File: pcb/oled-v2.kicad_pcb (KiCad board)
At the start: 2 copper layers, 89.5 x 39.5 mm, 26 parts, among them J1 OLED_128x32, U1 MOUDLE-SEEEDUINO-XIAO

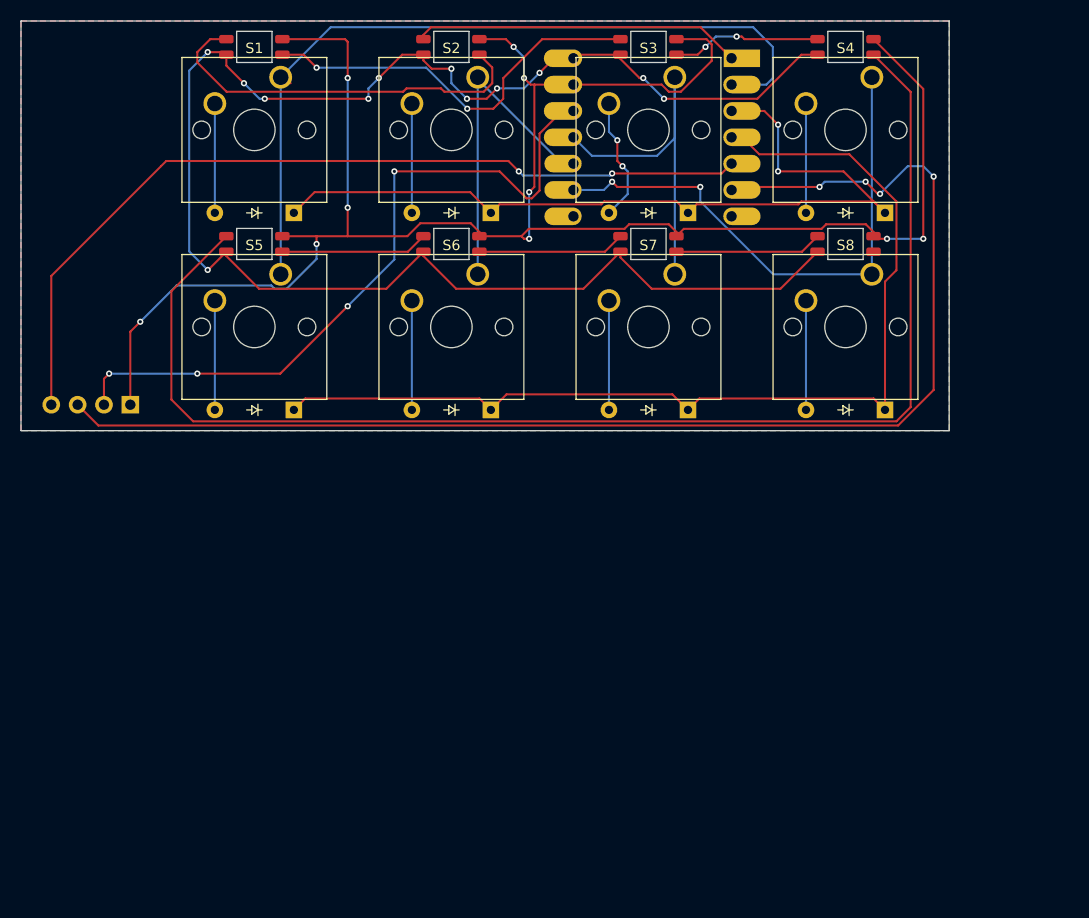
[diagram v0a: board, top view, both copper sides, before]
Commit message: turns out I had my GND wired to 5V - fixed now.
production/oled-v2.3mf = full CAD file
images updated
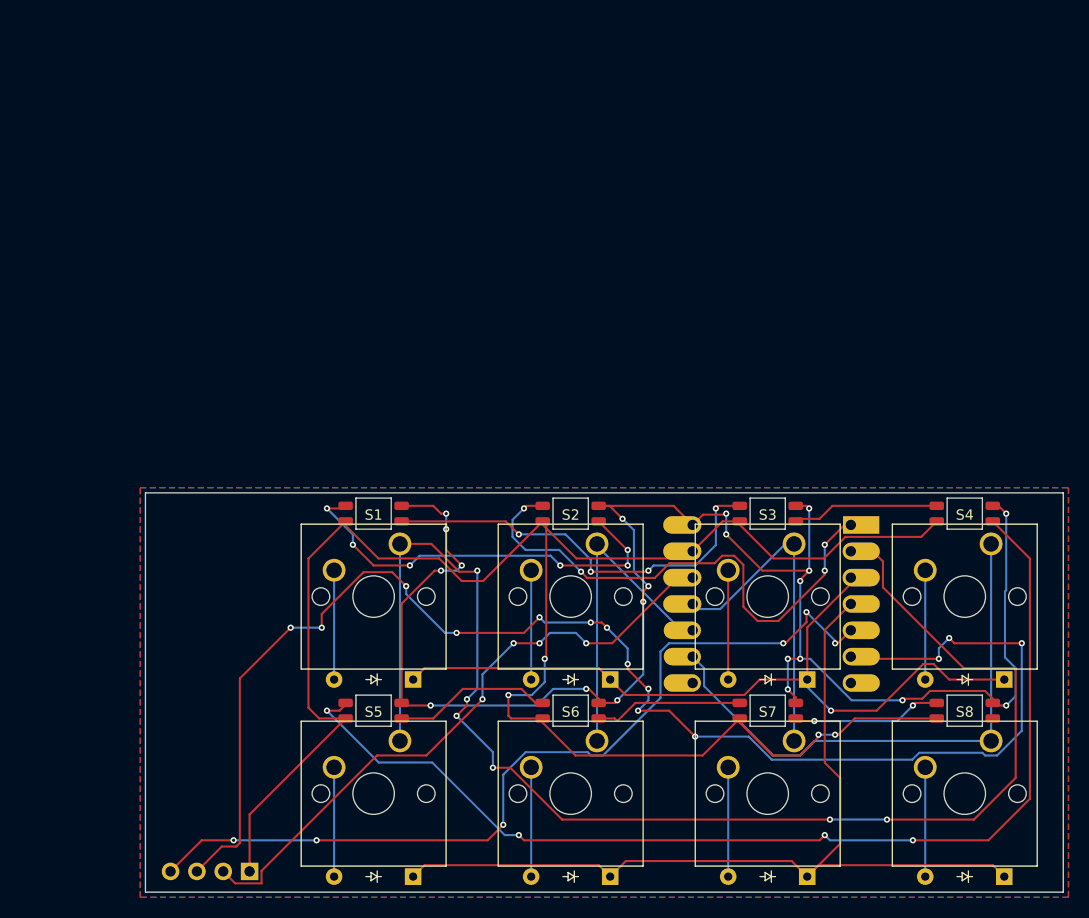
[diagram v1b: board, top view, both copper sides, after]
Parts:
- moved D1 46.4 mm to (99.3, 116.0)
- moved D10 46.4 mm to (114.5, 100.0)
- moved D11 46.4 mm to (133.5, 100.0)
- moved D12 46.4 mm to (152.5, 100.0)
- moved D13 46.4 mm to (95.5, 119.0)
- moved D14 46.4 mm to (114.5, 119.0)
- moved D15 46.4 mm to (133.5, 119.0)
- moved D16 46.4 mm to (152.5, 119.0)
- moved D2 46.4 mm to (118.3, 116.0)
- moved D3 46.4 mm to (137.3, 116.0)
- moved D4 46.4 mm to (156.3, 116.0)
- moved D5 46.4 mm to (99.3, 135.0)
- moved D6 46.4 mm to (118.3, 135.0)
- moved D7 46.4 mm to (137.3, 135.0)
- moved D8 46.4 mm to (156.3, 135.0)
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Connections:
- D10 pad 1: LED_GND -> 5V
- D10 pad 3: 5V -> LED_GND
- D11 pad 1: LED_GND -> 5V
- D11 pad 3: 5V -> LED_GND
- D12 pad 1: LED_GND -> 5V
- D12 pad 3: 5V -> LED_GND
- D13 pad 1: LED_GND -> 5V
- D13 pad 3: 5V -> LED_GND
- D14 pad 1: LED_GND -> 5V
- D14 pad 3: 5V -> LED_GND
- D15 pad 1: LED_GND -> 5V
- D15 pad 3: 5V -> LED_GND
- D16 pad 1: LED_GND -> 5V
- D16 pad 3: 5V -> LED_GND
- D9 pad 1: LED_GND -> 5V
- D9 pad 3: 5V -> LED_GND
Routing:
- net Col 0: track 77.7 -> 135.6 mm, vias 0 -> 6
- net Net-(D12-DOUT): track 126.1 -> 105.9 mm, vias 0 -> 4
- net LED0_DIN: track 31.7 -> 50.7 mm, vias 0 -> 4
- net OLED_SCL: track 127.2 -> 142.6 mm, vias 4 -> 14
- net LED_GND: track 190.8 -> 180.0 mm, vias 10 -> 4
- net Row 1: track 99.1 -> 89.3 mm
- net OLED_VCC: track 68.8 -> 60.9 mm
- net Row 0: track 82.0 -> 74.9 mm, vias 2 -> 1
- net Col 2: track 36.1 -> 31.6 mm
- net Net-(D10-DOUT): track 37.8 -> 40.0 mm, vias 0 -> 6
- net Net-(D3-A): track 12.0 -> 10.5 mm, vias 2 -> 0
- net Net-(D11-DIN): track 38.7 -> 40.0 mm, vias 2 -> 4
- net Net-(D13-DOUT): track 14.2 -> 15.3 mm
- net 5V: track 163.7 -> 162.9 mm, vias 12 -> 21
- net Col 3: track 52.6 -> 53.3 mm, vias 2 -> 0
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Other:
- board size 89.5 x 39.5 mm -> 88.5 x 38.5 mm

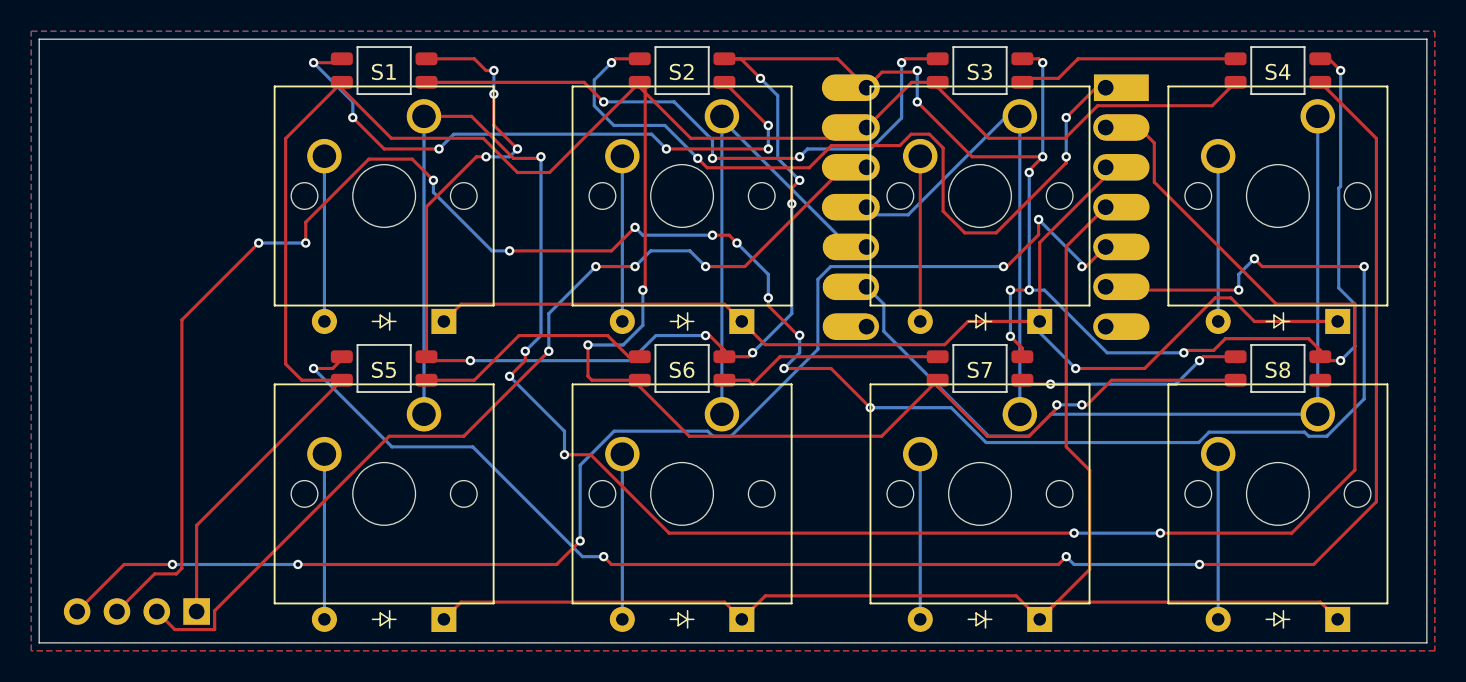
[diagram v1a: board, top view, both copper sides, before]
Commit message: rewired lights, needs checking through
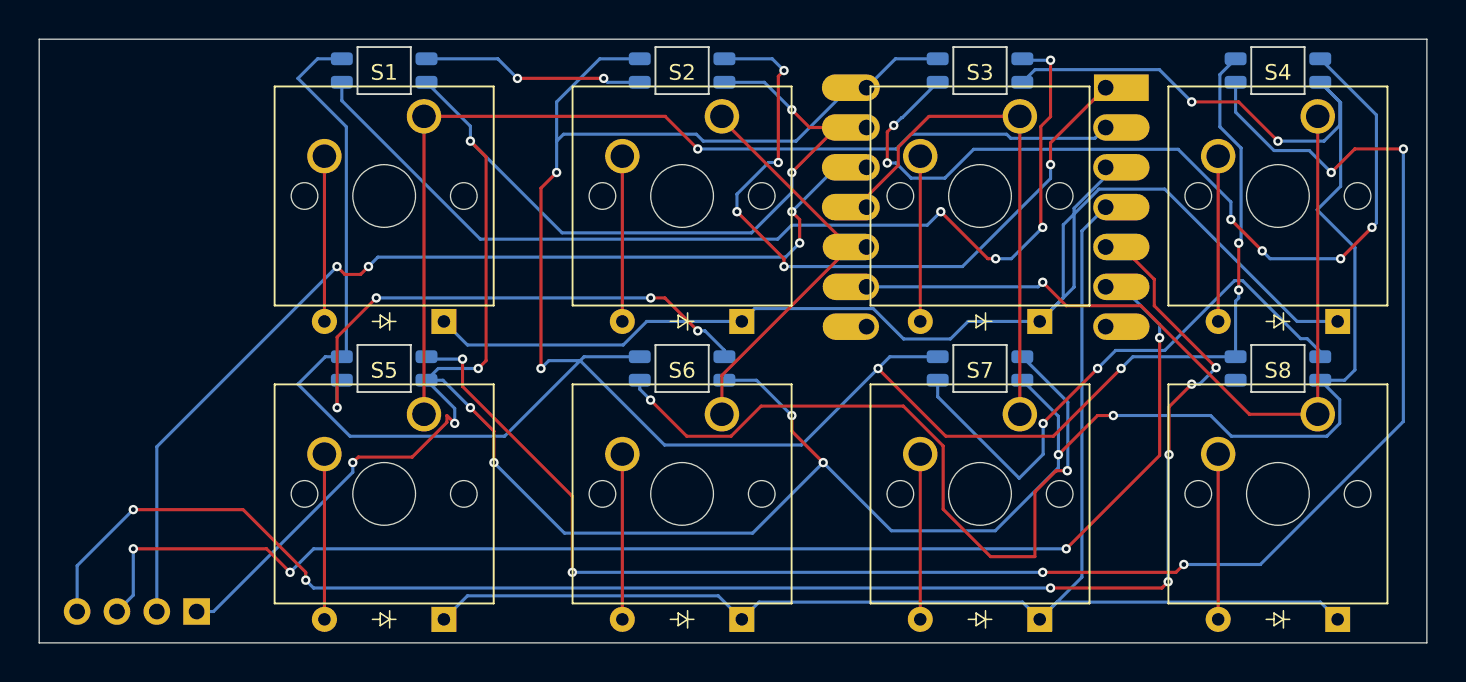
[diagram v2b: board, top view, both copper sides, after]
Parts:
- D10, D11, D12, D13, D14, D15, D16, D9: moved to B.Cu
- turned D10 to 180 degrees
- turned D11 to 180 degrees
- turned D12 to 180 degrees
- turned D13 to 180 degrees
- turned D14 to 180 degrees
- turned D15 to 180 degrees
- turned D16 to 180 degrees
- turned D9 to 180 degrees
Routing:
- net Col 0: track 135.6 -> 64.1 mm, vias 6 -> 1
- net OLED_SCL: track 142.6 -> 86.4 mm, vias 14 -> 4
- net LED_GND: track 180.0 -> 229.8 mm, vias 4 -> 14
- net Net-(D11-DOUT): track 14.2 -> 55.3 mm, vias 0 -> 6
- net Net-(D14-DOUT): track 14.4 -> 49.4 mm, vias 0 -> 2
- net Net-(D10-DOUT): track 40.0 -> 14.2 mm, vias 6 -> 2
- net Net-(D11-DIN): track 40.0 -> 65.1 mm
- net Net-(D15-DOUT): track 14.4 -> 36.2 mm
- net OLED_SDA: track 84.1 -> 102.9 mm, vias 6 -> 7
- net Net-(D13-DOUT): track 15.3 -> 33.9 mm, vias 0 -> 4
- net 5V: track 162.9 -> 178.8 mm, vias 21 -> 6
- net Row 0: track 74.9 -> 81.1 mm, vias 1 -> 0
- net LED0_DIN: track 50.7 -> 46.0 mm, vias 4 -> 5
- net OLED_VCC: track 60.9 -> 65.4 mm
- net Col 1: track 31.8 -> 27.9 mm
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- removed copper zone on B.Cu, net (none)
- removed copper zone on F.Cu, net (none)
